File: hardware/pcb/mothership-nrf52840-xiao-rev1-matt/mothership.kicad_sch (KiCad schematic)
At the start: 17 parts, among them J1 HRO TYPE-C-31-M-12, J2 USB_EXT_FFC_CABLE, J3 Screw_Terminal_01x01, J4 BOT_L, J5 BOT_R, J6 TOP_R, J7 TOP_L, U1 NCP361SN, U3 MCP23017x-x-SS, U4 MCP23017x-x-SS, U5 DT1452-02SO

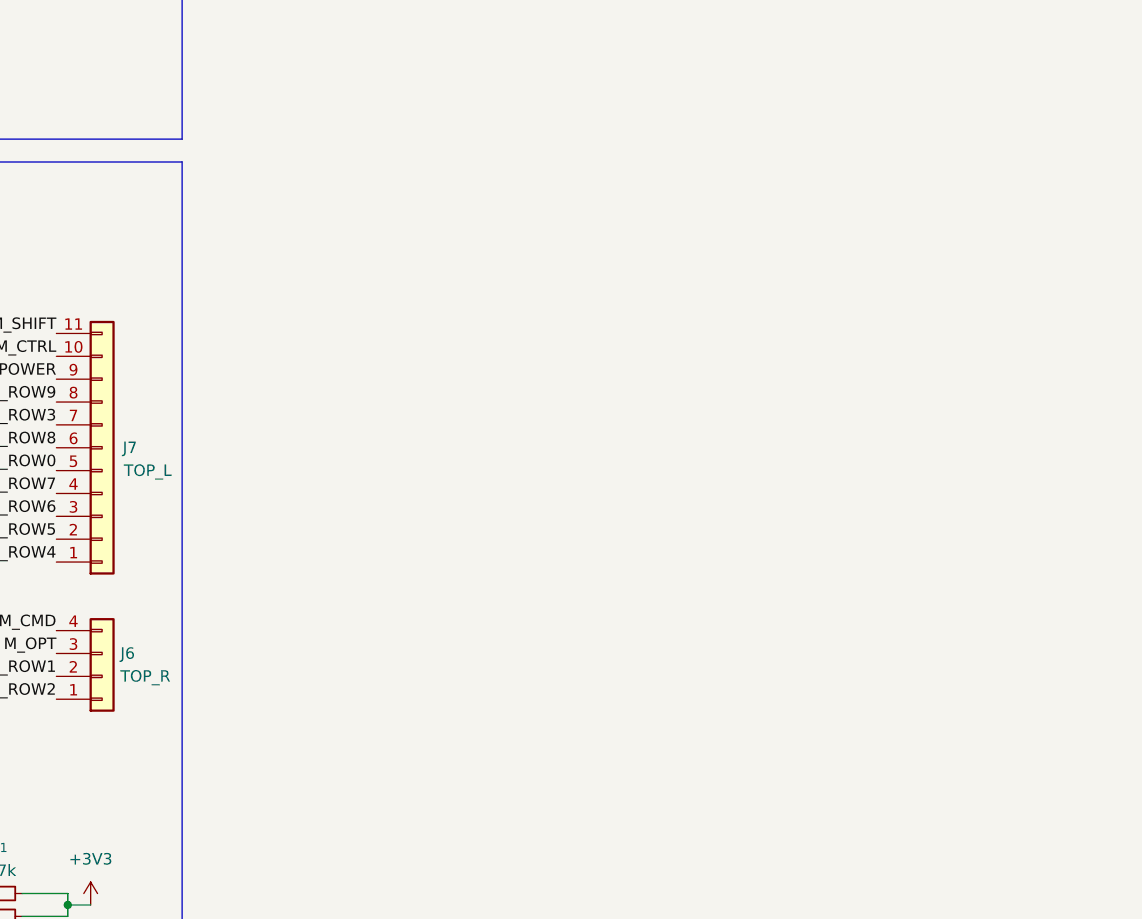
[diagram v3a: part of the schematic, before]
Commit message: sch: add encoder ec11 hardware debouncing + SPI connector
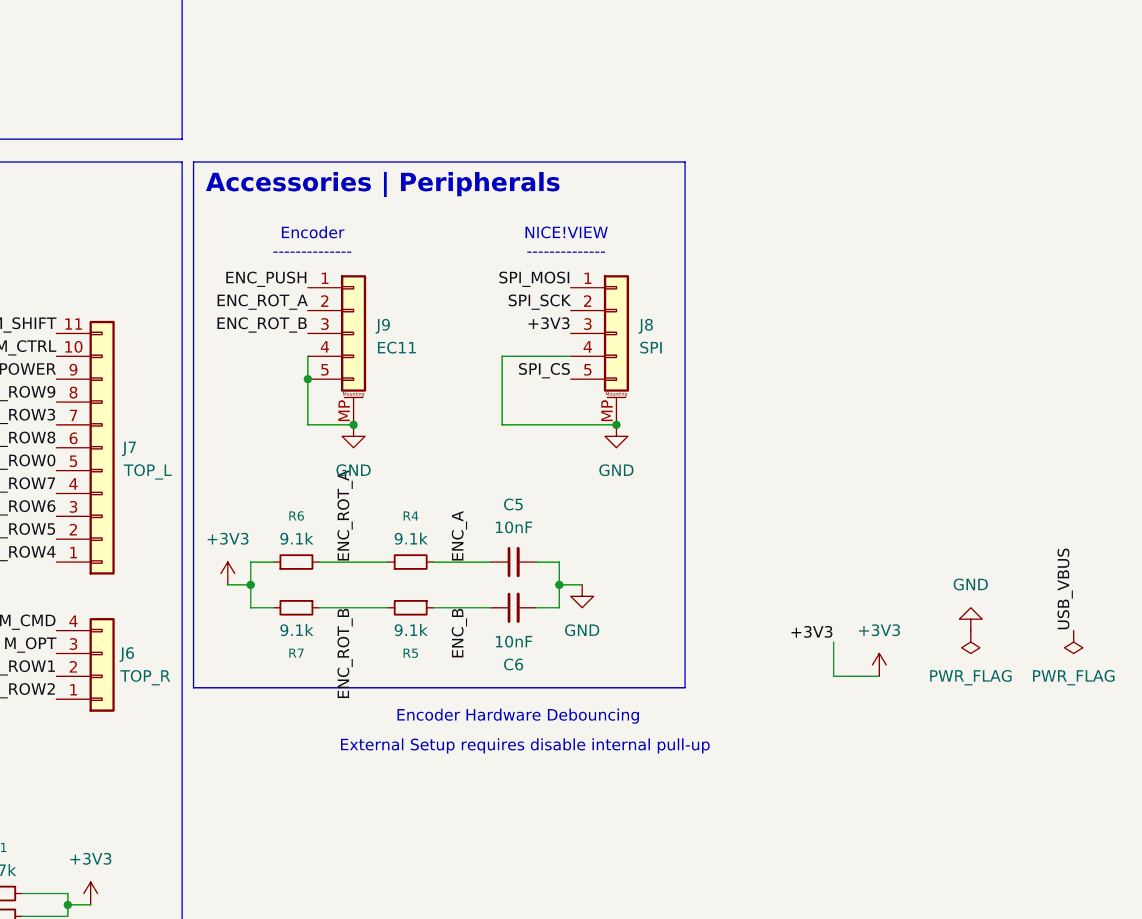
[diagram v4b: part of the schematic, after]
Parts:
- added C5, C6: 10nF, symbol A9M0330:C_Small
- added J8: SPI, symbol A9M0330:Conn_01x05_MountingPin
- added J9: EC11, symbol A9M0330:Conn_01x05_MountingPin
- added R4, R5, R6, R7: 9.1k, symbol A9M0330:R_Small
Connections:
- net +3V3: now also J8.3 (Pin_3), R6.1, R7.2
- net ENC_A: now also C5.1, R4.2
- net ENC_B: now also C6.1, R5.1
- net ENC_PUSH: now also J9.1 (Pin_1)
- net GND: now also C5.2, C6.2, J8.4 (Pin_4), J8.MP (MountPin), J9.4 (Pin_4), J9.5 (Pin_5), J9.MP (MountPin)
- new net ENC_ROT_A: J9.2 (Pin_2), R4.1, R6.2
- new net ENC_ROT_B: J9.3 (Pin_3), R5.2, R7.1
- new net SPI_CS: J8.5 (Pin_5)
- new net SPI_MOSI: J8.1 (Pin_1)
- new net SPI_SCK: J8.2 (Pin_2)
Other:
- note added: "Accessories | Peripherals"
- note added: "Encoder --------------"
- note added: "Encoder Hardware Debouncing"
- note added: "External Setup requires disable internal pull-up"
- note added: "NICE!VIEW --------------"

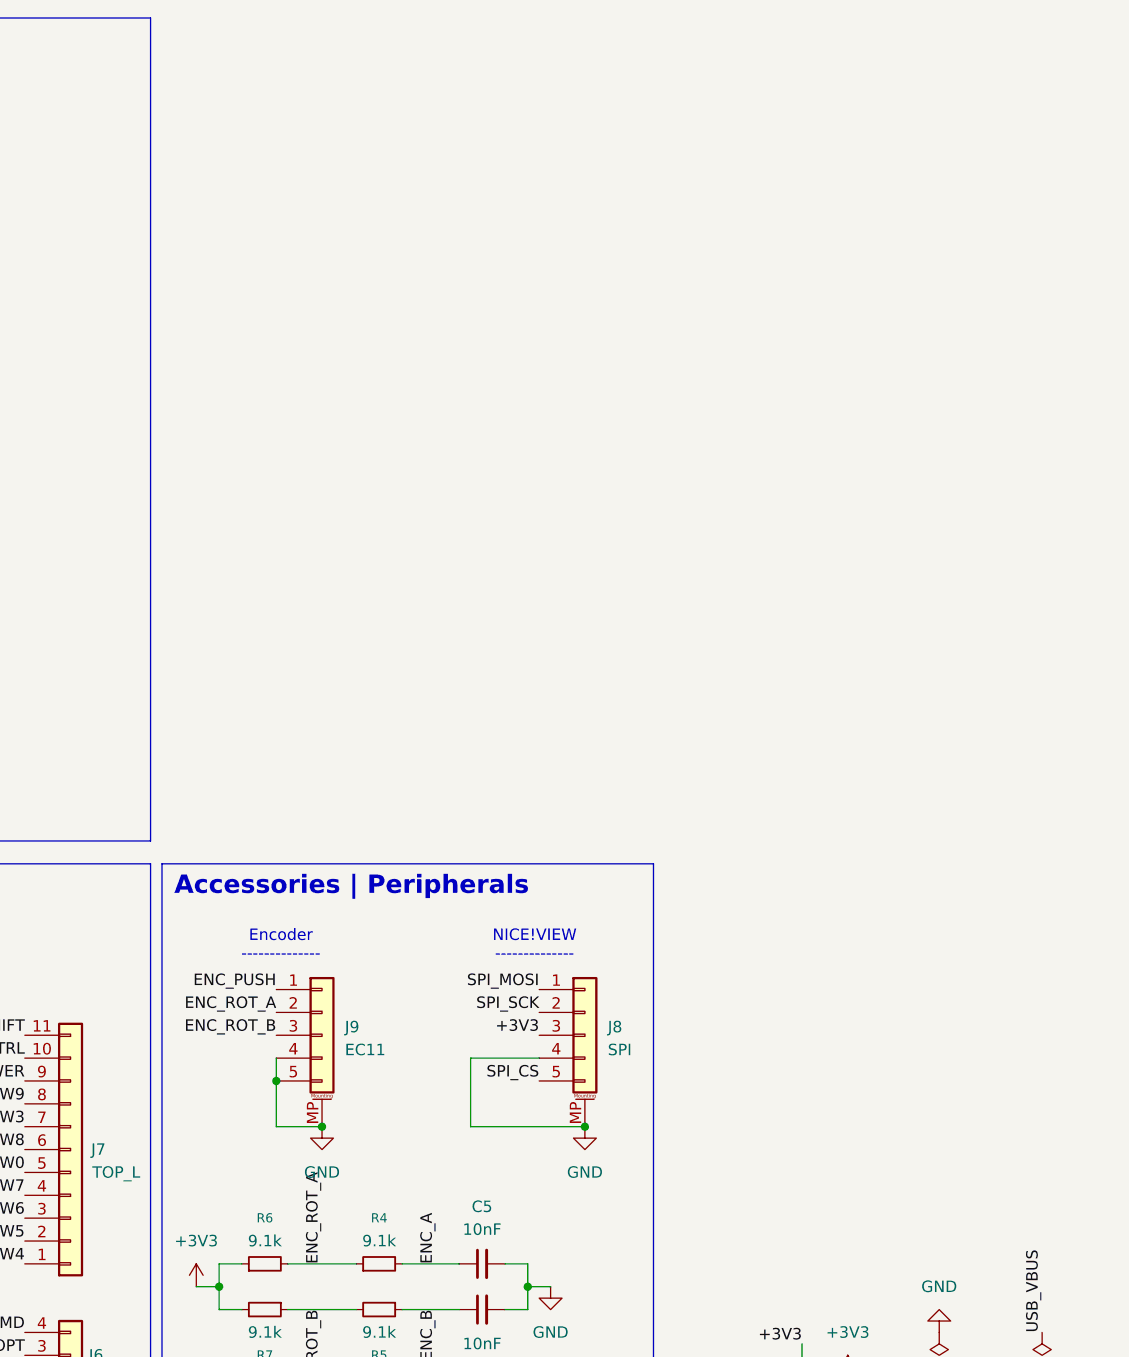
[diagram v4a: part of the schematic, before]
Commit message: sch: partial circuit for xiao mcu and battery
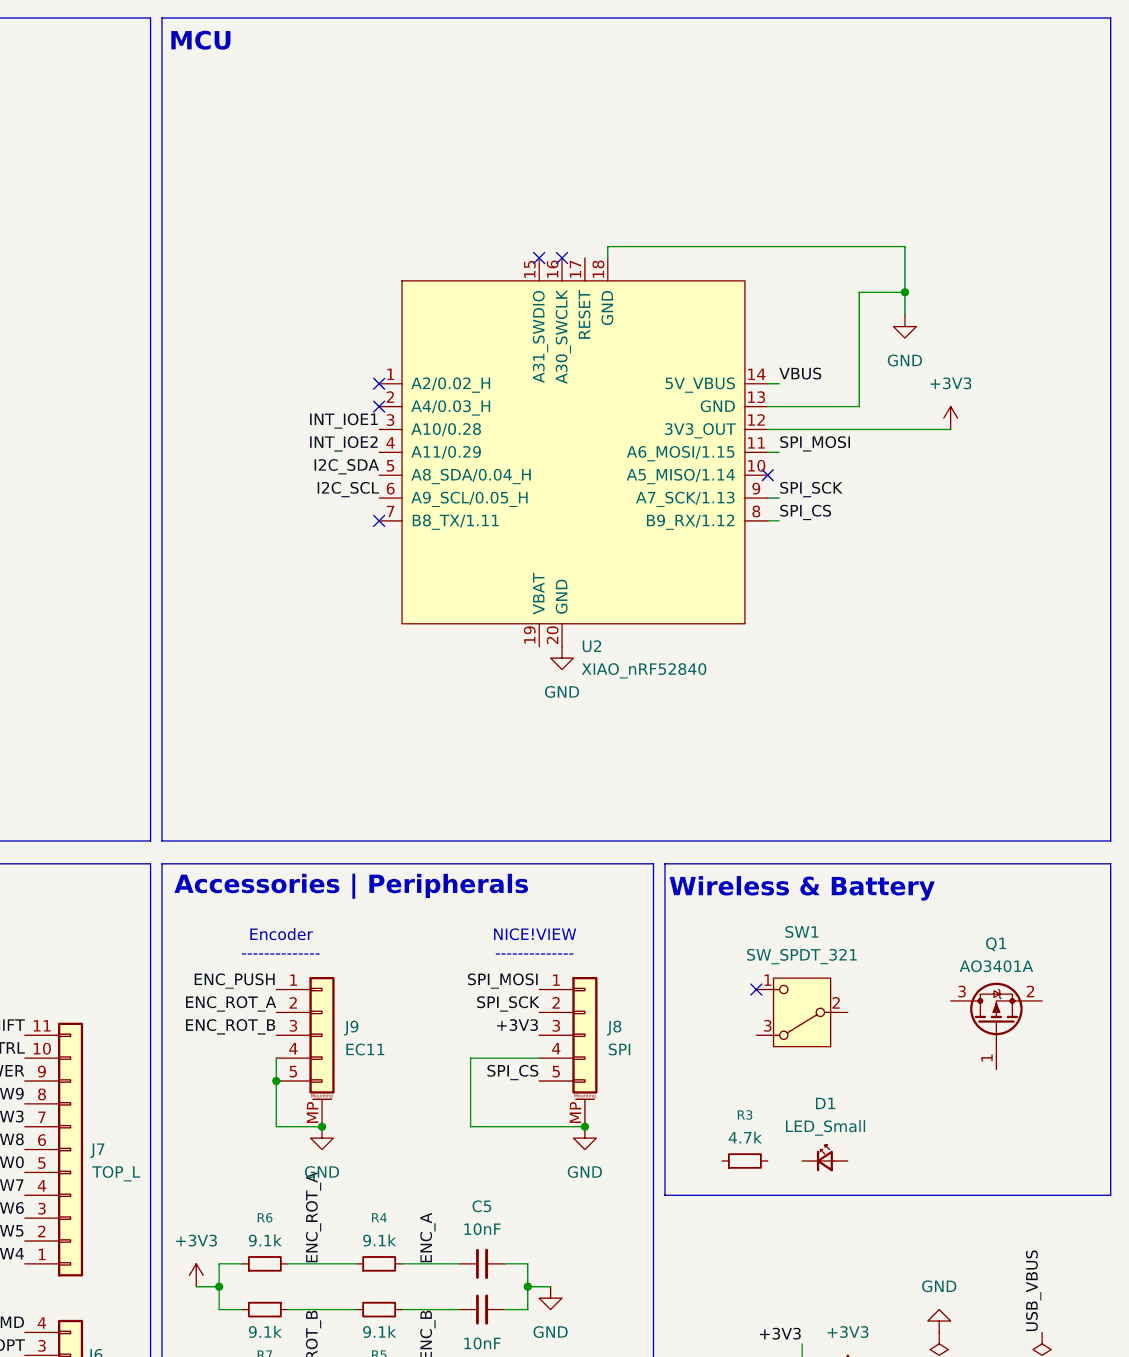
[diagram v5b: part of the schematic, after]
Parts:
- added D1: LED_Small, symbol A9M0330:LED_Small
- added Q1: AO3401A, Package_TO_SOT_SMD:SOT-23, symbol A9M0330:Transistor_FET__AO3401A
- added R3: 4.7k, symbol A9M0330:R_Small
- added SW1: SW_SPDT_321, symbol A9M0330:SW_SPDT_321
- added U2: XIAO_nRF52840, symbol A9M0330:MCU_Module__XIAO_nRF52840_NFC-NC
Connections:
- net +3V3: now also U2.12 (3V3_OUT)
- net GND: now also U2.13 (GND), U2.18 (GND), U2.20 (GND)
- net I2C_SCL: now also U2.6 (A9_SCL/0.05_H)
- net I2C_SDA: now also U2.5 (A8_SDA/0.04_H)
- net INT_IOE1: now also U2.3 (A10/0.28)
- net INT_IOE2: now also U2.4 (A11/0.29)
- net SPI_CS: now also U2.8 (B9_RX/1.12)
- net SPI_MOSI: now also U2.11 (A6_MOSI/1.15)
- net SPI_SCK: now also U2.9 (A7_SCK/1.13)
- net VBUS: now also U2.14 (5V_VBUS)
- no-connect marks 8 -> 15
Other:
- note added: "MCU"
- note added: "Wireless & Battery"
